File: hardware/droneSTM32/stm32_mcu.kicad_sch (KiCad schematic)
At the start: 31 parts, among them U101 STM32F103R8T6

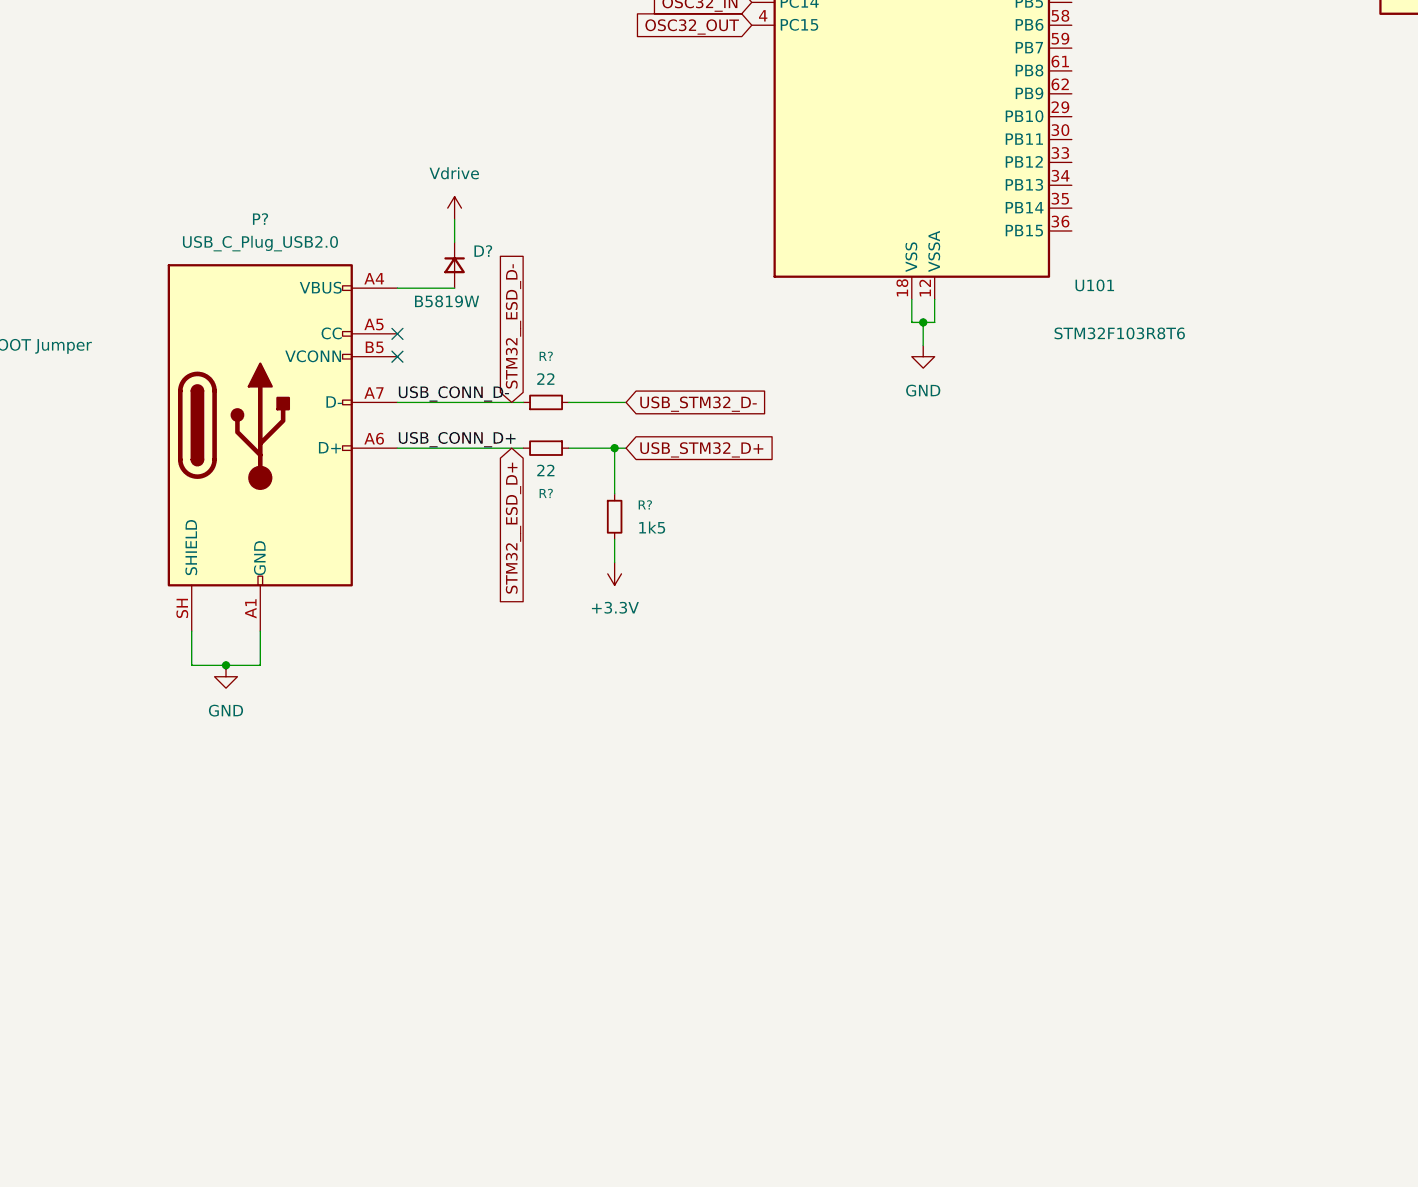
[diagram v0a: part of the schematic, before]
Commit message: feat: usb c replaced to usb micro b
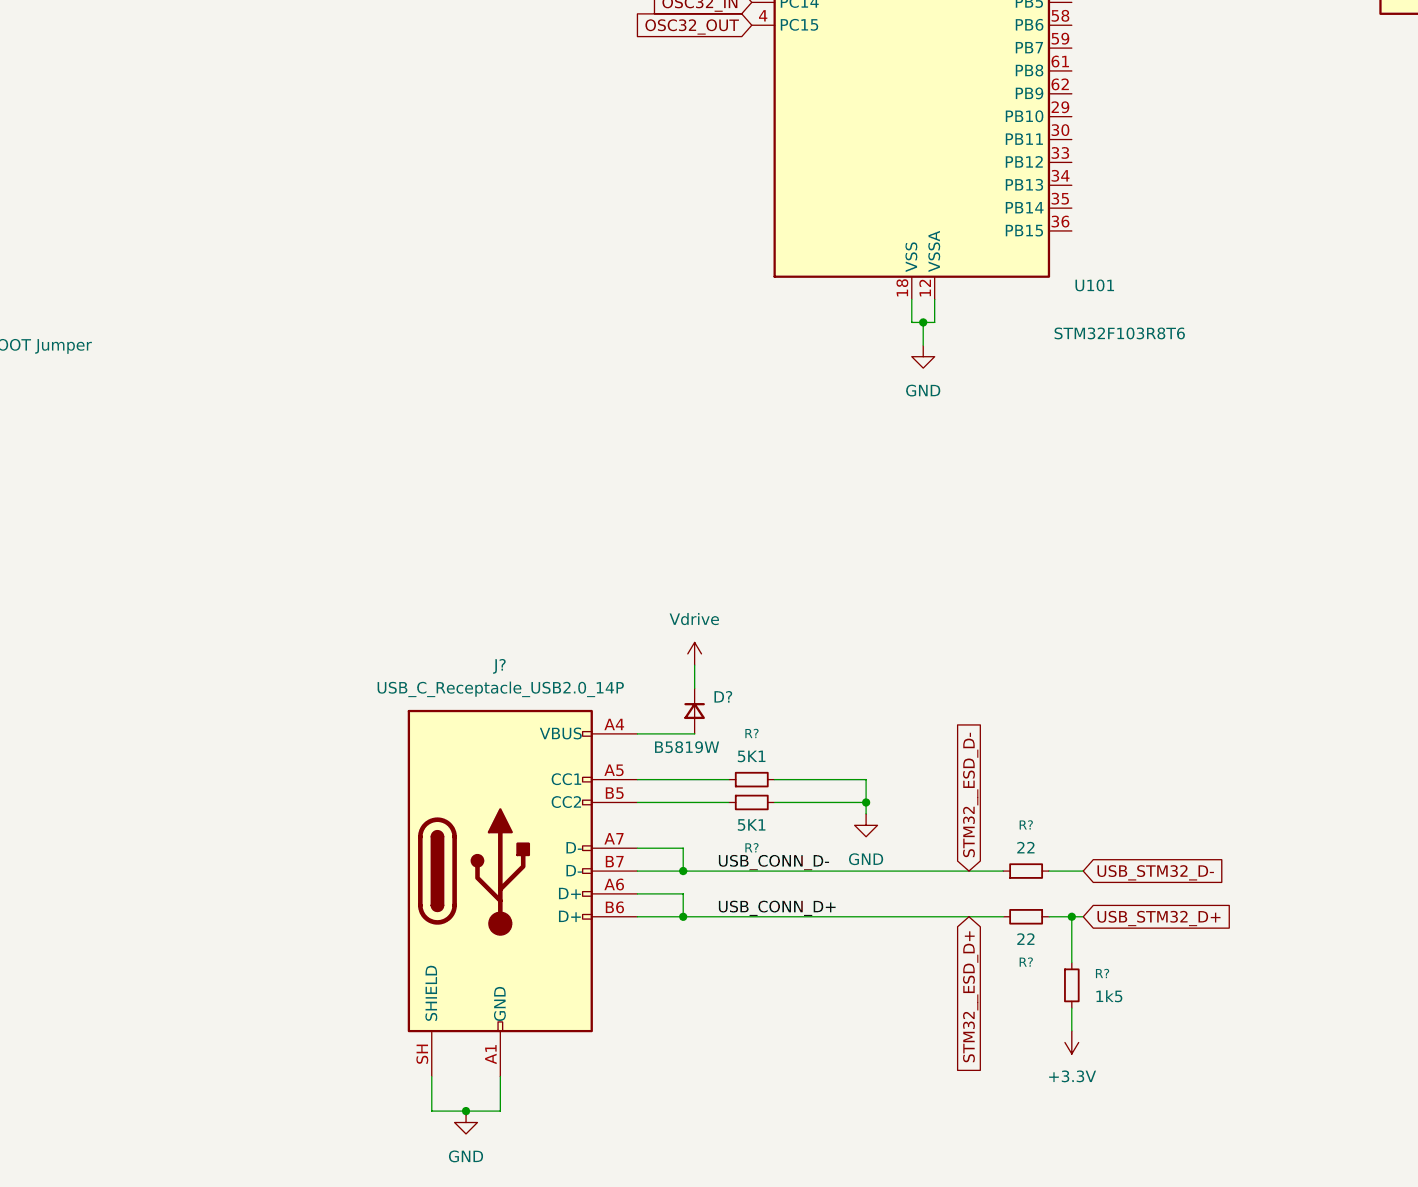
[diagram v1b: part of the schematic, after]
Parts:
- removed D?: B5819W, symbol Device:D_Small
- removed P?: USB_C_Plug_USB2.0, symbol Connector:USB_C_Plug_USB2.0
- removed R? (x2): 22, symbol Device:R_Small
- removed R?: 1k5, symbol Device:R_Small
- added D?: B5819W, symbol Device:D_Small
- added J?: USB_C_Receptacle_USB2.0_14P, symbol Connector:USB_C_Receptacle_USB2.0_14P
- added R? (x2): 22, symbol Device:R_Small
- added R? (x2): 5K1, symbol Device:R_Small
- added R?: 1k5, symbol Device:R_Small
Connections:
- net +3.3V: now also R?.2
- net GND: now also J?.A1 (GND), J?.A12 (GND), J?.B1 (GND), J?.B12 (GND), J?.SH (SHIELD), R?.2, R?.2
- net STM32__ESD_D+: now also J?.A6 (D+), J?.B6 (D+), R?.2
- net STM32__ESD_D-: now also J?.A7 (D-), J?.B7 (D-), R?.1
- net USB_STM32_D+: now also R?.1, R?.1
- net USB_STM32_D-: now also R?.2
- net Vdrive: now also D?.1 (K)
- new net: D?.2 (A), J?.A4 (VBUS), J?.A9 (VBUS), J?.B4 (VBUS), J?.B9 (VBUS)
- new net: J?.A5 (CC1), R?.1
- new net: J?.B5 (CC2), R?.1
- no-connect marks 2 -> 0

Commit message: commit mpu6050 update
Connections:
- net I2C2_SCL: now reaches U101.29 (PB10)
- net I2C2_SDA: now reaches U101.30 (PB11)
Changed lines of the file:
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@@
+		)
+	)
+	(global_label "I2C2_SDA"
+		(shape input)
+		(at 172.72 128.27 0)
+		(fields_autoplaced yes)
+		(effects
+			(font
+				(size 1.27 1.27)
+			)
+			(justify left)
+		)
+		(property "Intersheetrefs" "${INTERSHEET_REFS}"
+			(at 184.5347 128.27 0)
+			(hide yes)
+			(show_name no)
+			(do_not_autoplace no)
+			(effects
+				(font
+					(size 1.27 1.27)
+				)
+				(justify left)
+			)
 		)
 	)
@@
 			)
 		)
+	)
+	(global_label "I2C2_SCL"
+		(shape input)
+		(at 172.72 125.73 0)
+		(fields_autoplaced yes)
+		(effects
+			(font
+				(size 1.27 1.27)
+			)
+			(justify left)
+		)
+		(property "Intersheetrefs" "${INTERSHEET_REFS}"
+			(at 184.4742 125.73 0)
+			(hide yes)
+			(show_name no)
+			(do_not_autoplace no)
+			(effects
+				(font
+					(size 1.27 1.27)
+				)
+				(justify left)
+			)
+		)
